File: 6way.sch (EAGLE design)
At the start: 10 parts

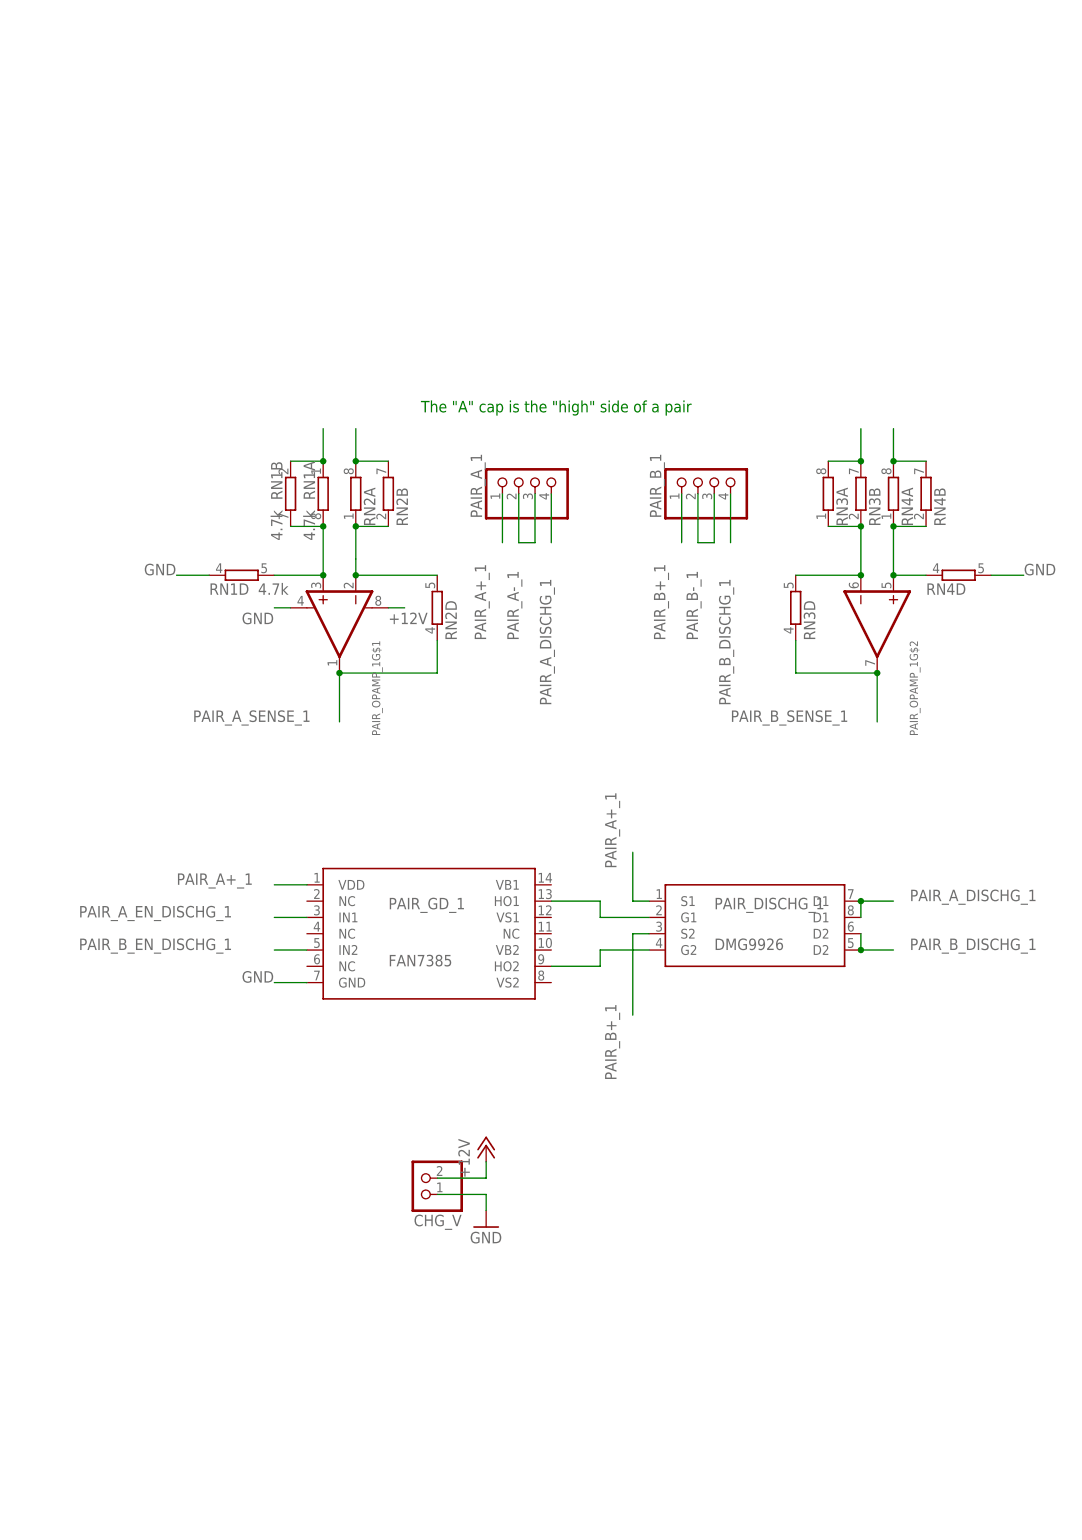
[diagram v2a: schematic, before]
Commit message: started to make the bootsrap circuit for the gate driver
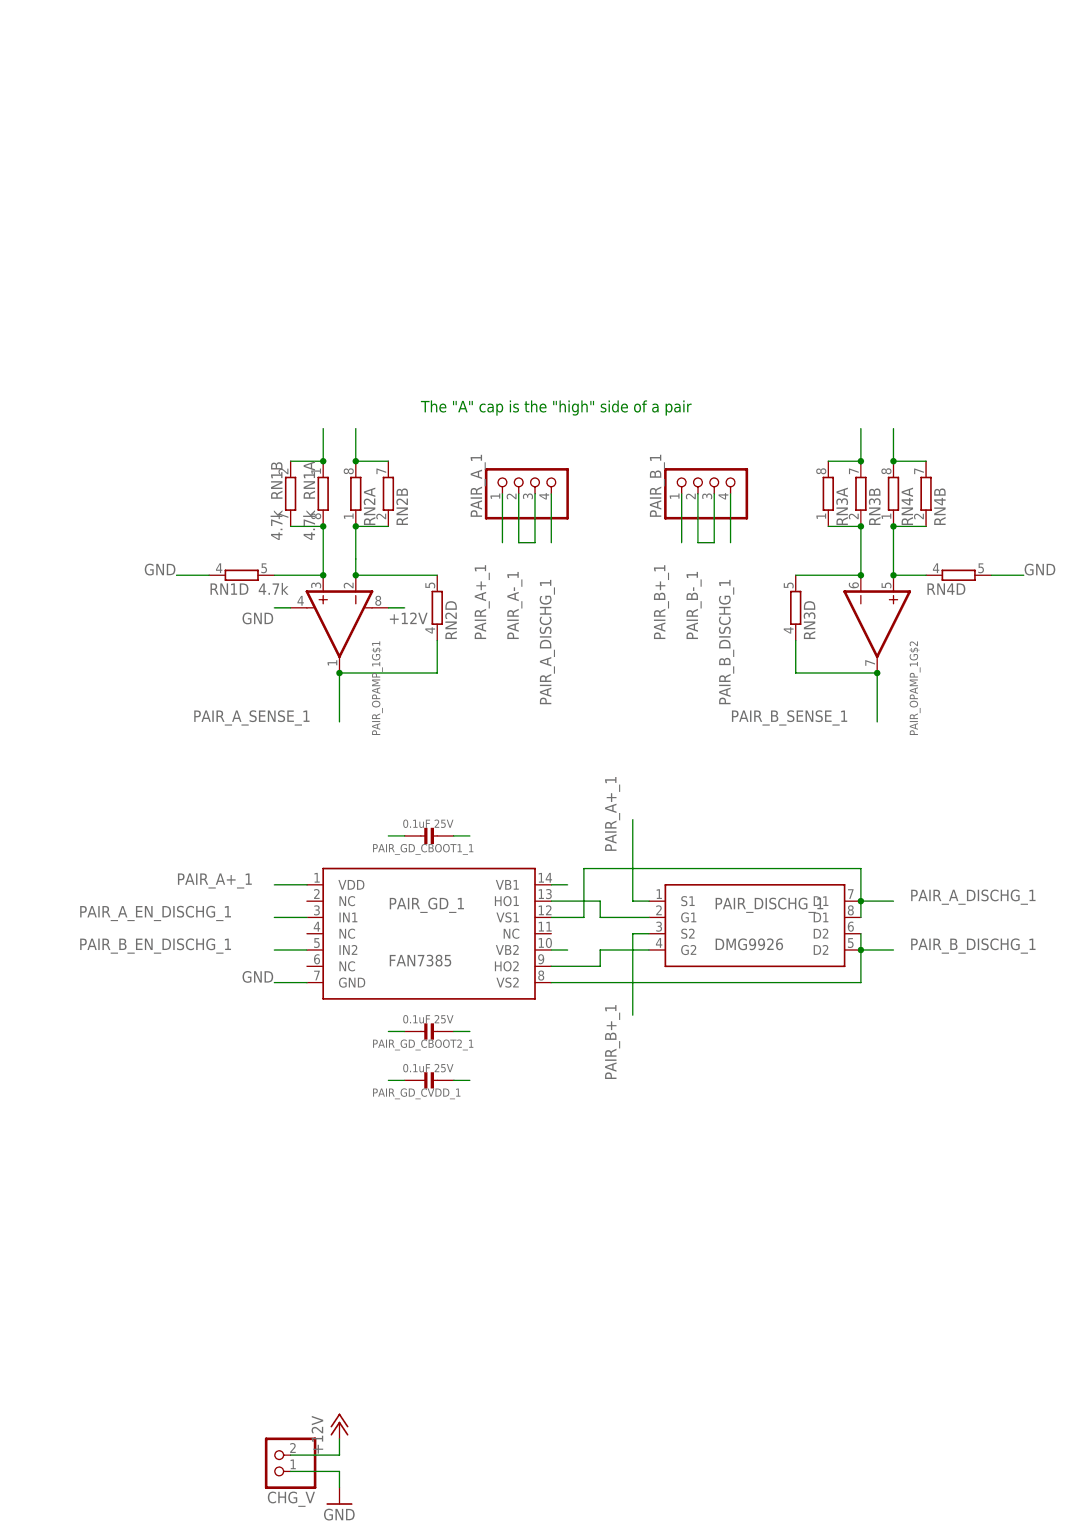
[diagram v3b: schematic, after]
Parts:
- added PAIR_GD_CBOOT1_1, PAIR_GD_CBOOT2_1, PAIR_GD_CVDD_1: 0.1uF 25V, microbuilder:CAP_CERAMIC0805
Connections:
- new net PAIR_GD_VB1_1: PAIR_GD_1.VB1, PAIR_GD_CBOOT1_1.P$2
- new net PAIR_GD_VB2_1: PAIR_GD_1.VB2, PAIR_GD_CBOOT2_1.P$2
- net GND: now also PAIR_GD_CVDD_1.P$1
- net PAIR_A+_1: now also PAIR_GD_CVDD_1.P$2
- net PAIR_A_DISCHG_1: now also PAIR_GD_1.VS1, PAIR_GD_CBOOT1_1.P$1
- net PAIR_B_DISCHG_1: now also PAIR_GD_1.VS2, PAIR_GD_CBOOT2_1.P$1
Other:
- moved on the sheet: CHG_V
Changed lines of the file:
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@@
 <part name="PAIR_GD_1" library="fan7385" deviceset="FAN7385" device=""/>
 <part name="PAIR_DISCHG_1" library="DMG9926" deviceset="DMG9926" device=""/>
+<part name="PAIR_GD_CBOOT1_1" library="microbuilder" deviceset="CAP_CERAMIC" device="0805" value="0.1uF 25V"/>
+<part name="PAIR_GD_CBOOT2_1" library="microbuilder" deviceset="CAP_CERAMIC" device="0805" value="0.1uF 25V"/>
+<part name="PAIR_GD_CVDD_1" library="microbuilder" deviceset="CAP_CERAMIC" device="0805" value="0.1uF 25V"/>
 </parts>
 <sheets>
@@
 </plain>
 <instances>
-<instance part="CHG_V" gate="G$1" x="2.54" y="7.62" rot="R180"/>
-<instance part="GND1" gate="1" x="12.7" y="0"/>
-<instance part="P+1" gate="1" x="12.7" y="12.7"/>
+<instance part="CHG_V" gate="G$1" x="-20.32" y="-35.56" rot="R180"/>
+<instance part="GND1" gate="1" x="-10.16" y="-43.18"/>
+<instance part="P+1" gate="1" x="-10.16" y="-30.48"/>
 <instance part="PAIR_A_1" gate="A" x="20.32" y="116.84" rot="R90"/>
 <instance part="PAIR_OPAMP_1" gate="G$1" x="-10.16" y="93.98" rot="R270"/>
@@
 <instance part="PAIR_GD_1" gate="G$1" x="0" y="45.72"/>
 <instance part="PAIR_DISCHG_1" gate="G$1" x="50.8" y="48.26"/>
+<instance part="PAIR_GD_CBOOT1_1" gate="G$1" x="2.54" y="60.96" smashed="yes" rot="R270">
+<attribute name="NAME" x="-5.08" y="58.42" size="1.27" layer="95" font="vector"/>
+<attribute name="VALUE" x="7.62" y="63.5" size="1.27" layer="96" font="vector" rot="R180"/>
+</instance>
+<instance part="PAIR_GD_CBOOT2_1" gate="G$1" x="2.54" y="30.48" smashed="yes" rot="R270">
+<attribute name="NAME" x="-5.08" y="27.94" size="1.27" layer="95" font="vector"/>
+<attribute name="VALUE" x="7.62" y="33.02" size="1.27" layer="96" font="vector" rot="R180"/>
+</instance>
+<instance part="PAIR_GD_CVDD_1" gate="G$1" x="2.54" y="22.86" smashed="yes" rot="R270">
+<attribute name="NAME" x="-5.08" y="20.32" size="1.27" layer="95" font="vector"/>
+<attribute name="VALUE" x="7.62" y="25.4" size="1.27" layer="96" font="vector" rot="R180"/>
+</instance>
 </instances>
 <busses>
@@
 <pinref part="CHG_V" gate="G$1" pin="2"/>
 <pinref part="P+1" gate="1" pin="+12V"/>
-<wire x1="5.08" y1="7.62" x2="12.7" y2="7.62" width="0.1524" layer="91"/>
-<wire x1="12.7" y1="7.62" x2="12.7" y2="10.16" width="0.1524" layer="91"/>
+<wire x1="-17.78" y1="-35.56" x2="-10.16" y2="-35.56" width="0.1524" layer="91"/>
+<wire x1="-10.16" y1="-35.56" x2="-10.16" y2="-33.02" width="0.1524" layer="91"/>
 </segment>
 <segment>
@@
 <segment>
 <pinref part="GND1" gate="1" pin="GND"/>
-<wire x1="12.7" y1="2.54" x2="12.7" y2="5.08" width="0.1524" layer="91"/>
+<wire x1="-10.16" y1="-40.64" x2="-10.16" y2="-38.1" width="0.1524" layer="91"/>
 <pinref part="CHG_V" gate="G$1" pin="1"/>
-<wire x1="12.7" y1="5.08" x2="5.08" y2="5.08" width="0.1524" layer="91"/>
+<wire x1="-10.16" y1="-38.1" x2="-17.78" y2="-38.1" width="0.1524" layer="91"/>
 </segment>
 <segment>
@@
 <wire x1="-15.24" y1="38.1" x2="-20.32" y2="38.1" width="0.1524" layer="91"/>
 <label x="-25.4" y="38.1" size="1.778" layer="95"/>
+</segment>
+<segment>
+<pinref part="PAIR_GD_CVDD_1" gate="G$1" pin="P$1"/>
+<wire x1="7.62" y1="22.86" x2="10.16" y2="22.86" width="0.1524" layer="91"/>
 </segment>
 </net>
@@
 <junction x="71.12" y="50.8"/>
 <label x="78.74" y="50.8" size="1.778" layer="95"/>
+<wire x1="71.12" y1="50.8" x2="71.12" y2="55.88" width="0.1524" layer="91"/>
+<wire x1="71.12" y1="55.88" x2="27.94" y2="55.88" width="0.1524" layer="91"/>
+<wire x1="27.94" y1="55.88" x2="27.94" y2="48.26" width="0.1524" layer="91"/>
+<pinref part="PAIR_GD_1" gate="G$1" pin="VS1"/>
+<wire x1="27.94" y1="48.26" x2="22.86" y2="48.26" width="0.1524" layer="91"/>
+</segment>
+<segment>
+<pinref part="PAIR_GD_CBOOT1_1" gate="G$1" pin="P$1"/>
+<wire x1="7.62" y1="60.96" x2="10.16" y2="60.96" width="0.1524" layer="91"/>
 </segment>
 </net>
@@
 <pinref part="PAIR_DISCHG_1" gate="G$1" pin="S1"/>
 <wire x1="38.1" y1="50.8" x2="35.56" y2="50.8" width="0.1524" layer="91"/>
-<wire x1="35.56" y1="50.8" x2="35.56" y2="58.42" width="0.1524" layer="91"/>
-<label x="33.02" y="55.88" size="1.778" layer="95" rot="R90"/>
+<wire x1="35.56" y1="50.8" x2="35.56" y2="63.5" width="0.1524" layer="91"/>
+<label x="33.02" y="58.42" size="1.778" layer="95" rot="R90"/>
 </segment>
 <segment>
@@
 <wire x1="-15.24" y1="53.34" x2="-20.32" y2="53.34" width="0.1524" layer="91"/>
 <label x="-35.56" y="53.34" size="1.778" layer="95"/>
+</segment>
+<segment>
+<pinref part="PAIR_GD_CVDD_1" gate="G$1" pin="P$2"/>
+<wire x1="0" y1="22.86" x2="-2.54" y2="22.86" width="0.1524" layer="91"/>
 </segment>
 </net>
@@
 <junction x="71.12" y="43.18"/>
 <label x="78.74" y="43.18" size="1.778" layer="95"/>
+<pinref part="PAIR_GD_1" gate="G$1" pin="VS2"/>
+<wire x1="22.86" y1="38.1" x2="71.12" y2="38.1" width="0.1524" layer="91"/>
+<wire x1="71.12" y1="38.1" x2="71.12" y2="43.18" width="0.1524" layer="91"/>
+</segment>
+<segment>
+<pinref part="PAIR_GD_CBOOT2_1" gate="G$1" pin="P$1"/>
+<wire x1="7.62" y1="30.48" x2="10.16" y2="30.48" width="0.1524" layer="91"/>
 </segment>
 </net>
@@
 </segment>
 </net>
+<net name="PAIR_GD_VB1_1" class="0">
+<segment>
+<pinref part="PAIR_GD_1" gate="G$1" pin="VB1"/>
+<wire x1="22.86" y1="53.34" x2="25.4" y2="53.34" width="0.1524" layer="91"/>
+</segment>
+<segment>
+<pinref part="PAIR_GD_CBOOT1_1" gate="G$1" pin="P$2"/>
+<wire x1="0" y1="60.96" x2="-2.54" y2="60.96" width="0.1524" layer="91"/>
+</segment>
+</net>
+<net name="PAIR_GD_VB2_1" class="0">
+<segment>
+<pinref part="PAIR_GD_1" gate="G$1" pin="VB2"/>
+<wire x1="22.86" y1="43.18" x2="25.4" y2="43.18" width="0.1524" layer="91"/>
+</segment>
+<segment>
+<pinref part="PAIR_GD_CBOOT2_1" gate="G$1" pin="P$2"/>
+<wire x1="0" y1="30.48" x2="-2.54" y2="30.48" width="0.1524" layer="91"/>
+</segment>
+</net>

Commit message: Bus for the sense/control signals
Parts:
- added PAIR_GD_DBOOT1_1, PAIR_GD_DBOOT2_1: (no value), microbuilder:DIODESOT23_WIDE
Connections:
- net PAIR_A+_1: now also PAIR_GD_DBOOT1_1.A, PAIR_GD_DBOOT2_1.A
- net PAIR_GD_VB1_1: now also PAIR_GD_DBOOT1_1.C
- net PAIR_GD_VB2_1: now also PAIR_GD_DBOOT2_1.C
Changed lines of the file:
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@@
 <part name="PAIR_GD_CBOOT2_1" library="microbuilder" deviceset="CAP_CERAMIC" device="0805" value="0.1uF 25V"/>
 <part name="PAIR_GD_CVDD_1" library="microbuilder" deviceset="CAP_CERAMIC" device="0805" value="0.1uF 25V"/>
+<part name="PAIR_GD_DBOOT2_1" library="microbuilder" deviceset="DIODE" device="SOT23_WIDE"/>
+<part name="PAIR_GD_DBOOT1_1" library="microbuilder" deviceset="DIODE" device="SOT23_WIDE"/>
 </parts>
 <sheets>
 <sheet>
 <plain>
-<text x="2.54" y="127" size="1.778" layer="91">The "A" cap is the "high" side of a pair</text>
+<text x="2.54" y="127" size="1.778" layer="97">The "A" cap is the "high" side of a pair</text>
 </plain>
 <instances>
@@
 <attribute name="VALUE" x="7.62" y="25.4" size="1.27" layer="96" font="vector" rot="R180"/>
 </instance>
+<instance part="PAIR_GD_DBOOT2_1" gate="G$1" x="-12.7" y="30.48" smashed="yes">
+<attribute name="NAME" x="-20.32" y="33.02" size="1.27" layer="95"/>
+<attribute name="VALUE" x="-15.24" y="26.67" size="1.27" layer="96"/>
+</instance>
+<instance part="PAIR_GD_DBOOT1_1" gate="G$1" x="-12.7" y="60.96" smashed="yes">
+<attribute name="NAME" x="-20.32" y="63.5" size="1.27" layer="95"/>
+<attribute name="VALUE" x="-15.24" y="57.15" size="1.27" layer="96"/>
+</instance>
 </instances>
 <busses>
+<bus name="PAIR_CTRL_1:PAIR_A_SENSE_1,PAIR_B_SENSE_1,PAIR_A_EN_DISCHG_1,PAIR_B_EN_DISCHG_1">
+<segment>
+<wire x1="-55.88" y1="78.74" x2="-55.88" y2="63.5" width="0.762" layer="92"/>
+<label x="-58.42" y="63.5" size="1.778" layer="95" rot="R90"/>
+</segment>
+</bus>
 </busses>
 <nets>
@@
 <junction x="-10.16" y="86.36"/>
 <label x="-33.02" y="78.74" size="1.778" layer="95"/>
+<wire x1="-48.26" y1="78.74" x2="-10.16" y2="78.74" width="0.1524" layer="91"/>
+<wire x1="-55.88" y1="78.74" x2="-48.26" y2="78.74" width="0.1524" layer="91"/>
 </segment>
 </net>
@@
 <wire x1="0" y1="22.86" x2="-2.54" y2="22.86" width="0.1524" layer="91"/>
 </segment>
+<segment>
+<pinref part="PAIR_GD_DBOOT1_1" gate="G$1" pin="A"/>
+<wire x1="-15.24" y1="60.96" x2="-20.32" y2="60.96" width="0.1524" layer="91"/>
+</segment>
+<segment>
+<pinref part="PAIR_GD_DBOOT2_1" gate="G$1" pin="A"/>
+<wire x1="-15.24" y1="30.48" x2="-20.32" y2="30.48" width="0.1524" layer="91"/>
+</segment>
 </net>
 <net name="PAIR_B-_1" class="2">
@@
 <label x="50.8" y="78.74" size="1.778" layer="95"/>
 </segment>
+<segment>
+<wire x1="-48.26" y1="76.2" x2="-40.64" y2="76.2" width="0.1524" layer="91"/>
+<label x="-40.64" y="76.2" size="1.778" layer="95"/>
+<wire x1="-55.88" y1="76.2" x2="-48.26" y2="76.2" width="0.1524" layer="91"/>
+</segment>
 </net>
 <net name="N$1" class="0">
@@
 <label x="-50.8" y="48.26" size="1.778" layer="95"/>
 </segment>
+<segment>
+<wire x1="-55.88" y1="73.66" x2="-45.72" y2="73.66" width="0.1524" layer="91"/>
+<label x="-45.72" y="73.66" size="1.778" layer="95"/>
+</segment>
 </net>
 <net name="PAIR_B_EN_DISCHG_1" class="0">
@@
 <wire x1="-15.24" y1="43.18" x2="-20.32" y2="43.18" width="0.1524" layer="91"/>
 <label x="-50.8" y="43.18" size="1.778" layer="95"/>
+</segment>
+<segment>
+<wire x1="-55.88" y1="71.12" x2="-48.26" y2="71.12" width="0.1524" layer="91"/>
+<label x="-48.26" y="71.12" size="1.778" layer="95"/>
 </segment>
 </net>
@@
 <pinref part="PAIR_GD_CBOOT1_1" gate="G$1" pin="P$2"/>
 <wire x1="0" y1="60.96" x2="-2.54" y2="60.96" width="0.1524" layer="91"/>
+<pinref part="PAIR_GD_DBOOT1_1" gate="G$1" pin="C"/>
+<wire x1="-10.16" y1="60.96" x2="-2.54" y2="60.96" width="0.1524" layer="91"/>
 </segment>
 </net>
@@
 <pinref part="PAIR_GD_CBOOT2_1" gate="G$1" pin="P$2"/>
 <wire x1="0" y1="30.48" x2="-2.54" y2="30.48" width="0.1524" layer="91"/>
-</segment>
-</net>
+<pinref part="PAIR_GD_DBOOT2_1" gate="G$1" pin="C"/>
+<wire x1="-10.16" y1="30.48" x2="-2.54" y2="30.48" width="0.1524" layer="91"/>
+</segment>
+</net>
